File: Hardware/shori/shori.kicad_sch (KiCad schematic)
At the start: 50 parts, among them J1 Conn_02x03_Top_Bottom, J2 SWD_Header, J3 UART_Header, J5 AudioJack3, U1 STM32F405RGT6, U2 AP2112K-3.3, U3 PCM3060PWR, U4 NE5532, Y1 16MHz

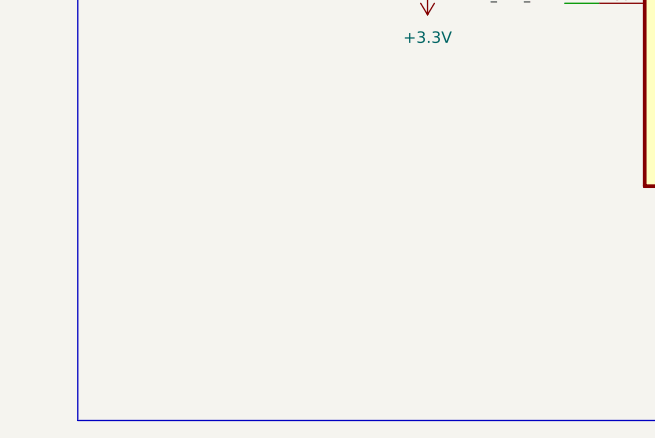
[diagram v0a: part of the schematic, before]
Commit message: Proper Border outline made for shori
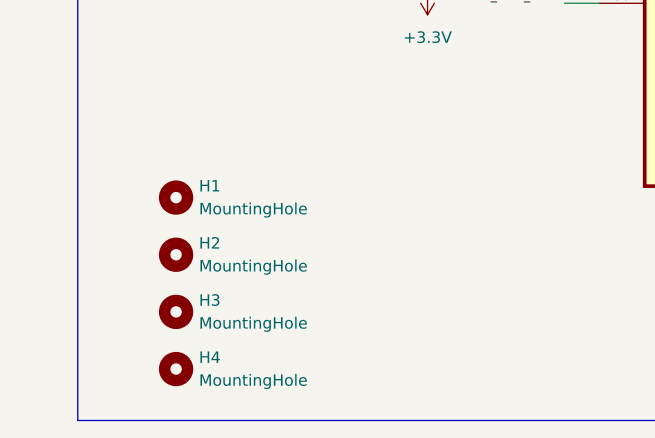
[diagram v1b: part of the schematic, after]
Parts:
- added H1, H2, H3, H4: MountingHole, MountingHole:MountingHole_3mm, symbol Mechanical:MountingHole

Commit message: saved previous commit
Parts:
- removed J1: Conn_02x03_Top_Bottom, Connector_IDC:IDC-Header_2x03_P2.54mm_Vertical, symbol Connector_Generic:Conn_02x03_Top_Bottom
- removed U1: STM32F405RGT6, My footprints:QFP50P1200X1200X160-64N, symbol STM32F4:STM32F405RGT6
- removed U2: AP2112K-3.3, Package_TO_SOT_SMD:SOT-23-5, symbol Regulator_Linear:AP2112K-3.3
- added C30: 10uF, Capacitor_SMD:C_0805_2012Metric, symbol Device:C
- added J1, J4, J6: Conn_01x03, Connector_JST:JST_EH_S3B-EH_1x03_P2.50mm_Horizontal, symbol Connector_Generic:Conn_01x03
- added U2: STM32H750VBTx, Package_QFP:LQFP-100_14x14mm_P0.5mm, symbol MCU_ST_STM32H7:STM32H750VBTx
- added U5: TPS73733DCQR, MyFootprints:IC_TPS73733DCQR, symbol TI LDO:TPS73733DCQR
- C10: value 10uF -> 100uF
- C3: value 10μF -> 4.7uF
- J3: footprint Connector_JST:JST_XH_B4B-XH-A_1x04_P2.50mm_Vertical -> Connector_JST:JST_XH_S4B-XH-A-1_1x04_P2.50mm_Horizontal
- U3: footprint My footprints:SOP65P640X120-28N -> MyFootprints:SOP65P640X120-28N
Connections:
- net NRST is gone; now on net BOOT0_R: C12.1, U3.15 (~{RST})
- net +3.3V: now also C30.1, U5.2 (OUT)
- net +3.3VA: now also U2.21 (VDDA)
- net BOOT0_R: now also U2.14 (NRST), U2.94 (BOOT0)
- net GND: now also C30.2, U2.10 (VSS), U2.100 (VDD), U2.11 (VDD), U2.19 (VSSA), U2.26 (VSS), U2.27 (VDD), U2.49 (VSS), U2.50 (VDD), U2.74 (VSS), U2.75 (VDD), U2.99 (VSS), U5.3 (GND_3), U5.6 (GND_6)
- net I2C_SCL: now also U2.46 (PB10)
- net I2C_SDA: now also U2.47 (PB11)
- net I2S_ADC_DATA: now also U2.53 (PB14)
- net I2S_BCLK: now also U2.51 (PB12)
- net I2S_DAC_DATA: now also U2.54 (PB15)
- net I2S_LRCLK: now also U2.52 (PB13)
- net I2S_MCLK: now also U2.63 (PC6)
- net SWCLK: now also U2.72 (PA13)
- net SWDIO: now also U2.76 (PA14)
- net UART_RX: now also J3.2 (Pin_2), U2.23 (PA1); no longer J3.3 (Pin_3)
- net UART_TX: now also J3.3 (Pin_3), U2.22 (PA0); no longer J3.2 (Pin_2)
- net VCAP_1: now also U2.48 (VCAP)
- net VCAP_2: now also U2.73 (VCAP)
- net at C3.1, D1.1 (K): now also U5.1 (IN), U5.5 (EN)
- no-connect marks 43 -> 6
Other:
- note added: "Shoyu Connectors: Power + AudioIn + AudioOut"
- note removed: "Main IDC Ribbon connector"
- moved on the sheet: C1, C10, C11, C12, C13, C14, C15, C16, C17, C18, C19, C2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

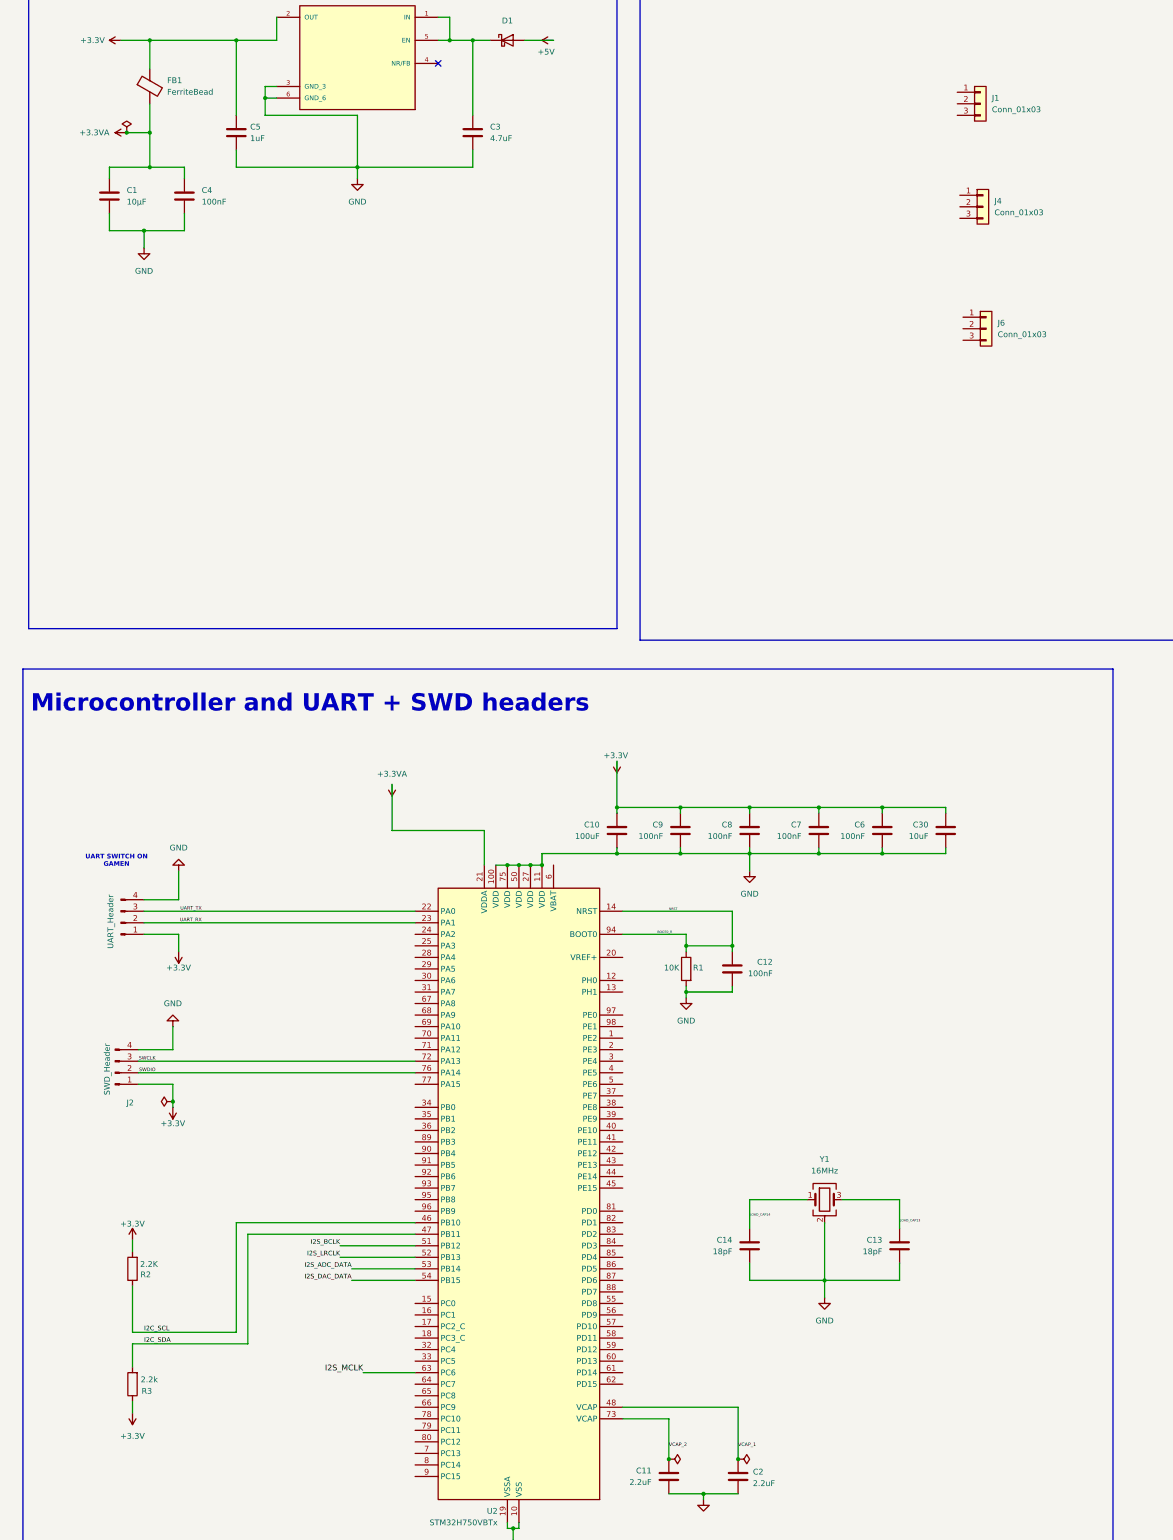
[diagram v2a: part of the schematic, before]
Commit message: Rev 2 mcu data lines and new shoyu molex connectors
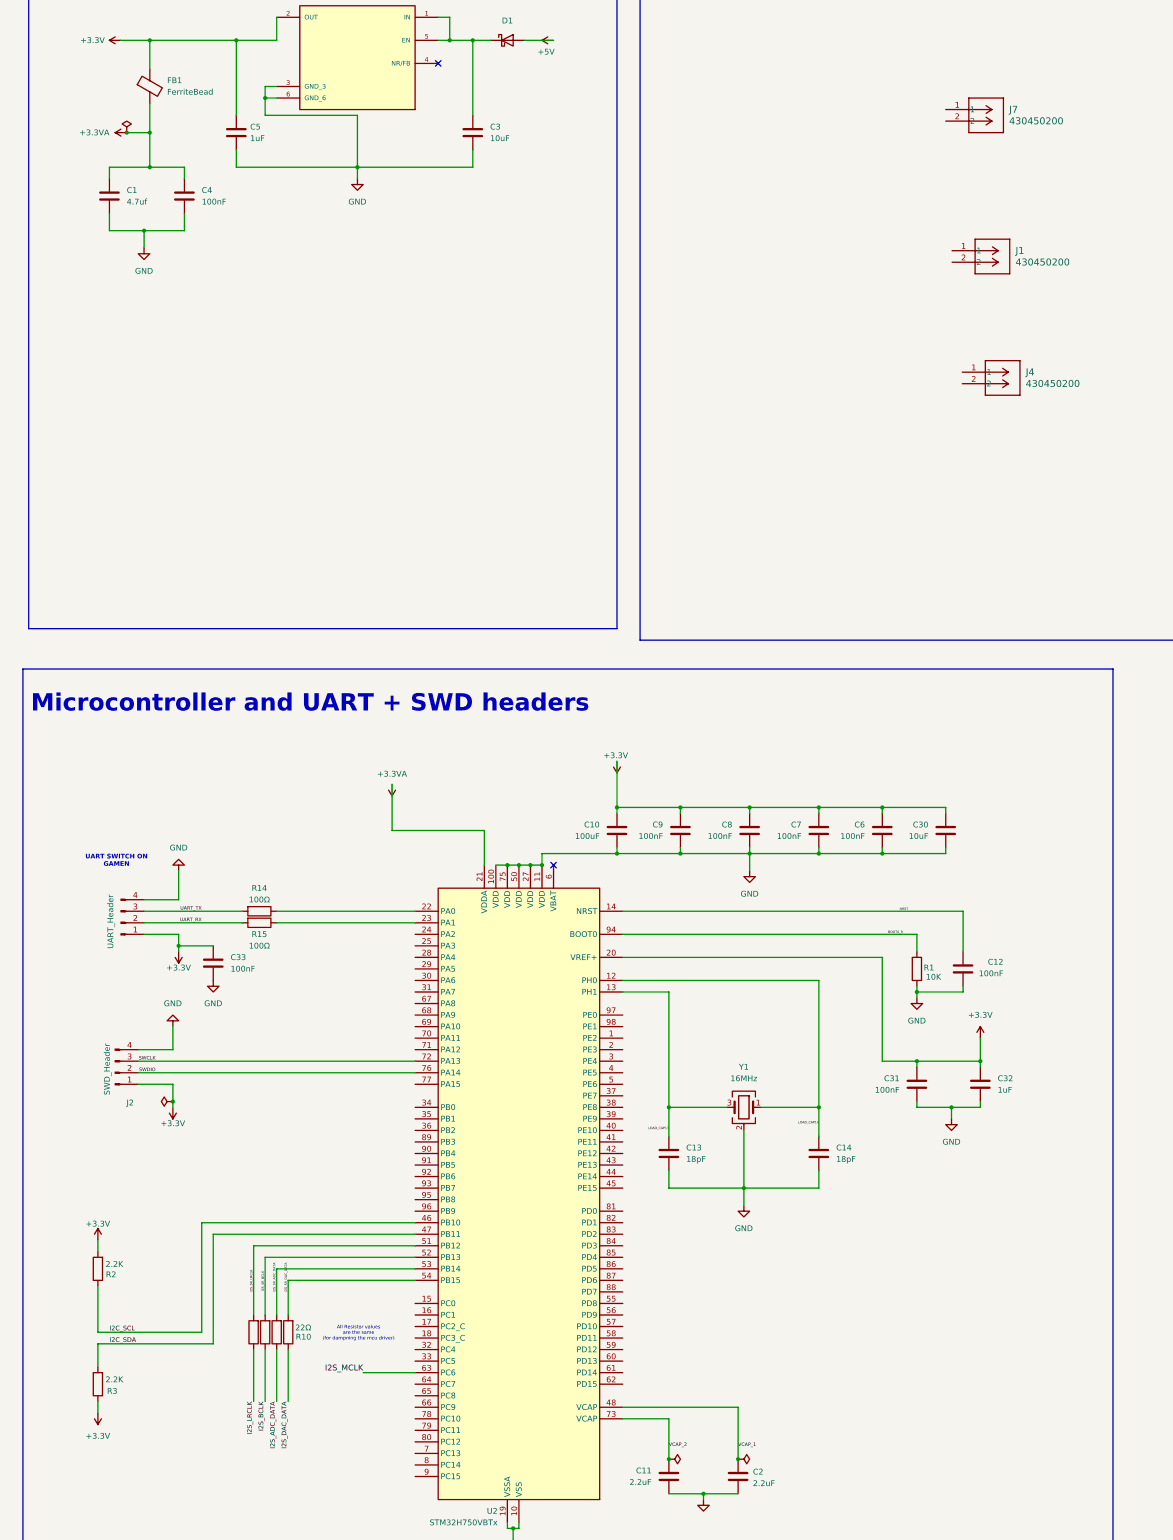
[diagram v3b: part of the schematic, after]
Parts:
- removed J1, J4, J6: Conn_01x03, Connector_JST:JST_EH_S3B-EH_1x03_P2.50mm_Horizontal, symbol Connector_Generic:Conn_01x03
- added C31: 100nF, Capacitor_SMD:C_0805_2012Metric, symbol Device:C
- added C32: 1uF, Capacitor_SMD:C_0805_2012Metric, symbol Device:C
- added C33: 100nF, symbol Device:C
- added J1, J4, J7: 430450200, MyFootprints:CONN_SD-43045-001_02_MOL, symbol MyConnectors:430450200
- added R10: 22Ω, Resistor_SMD:R_0805_2012Metric, symbol Device:R
- added R11, R12, R13: 22o, Resistor_SMD:R_0805_2012Metric, symbol Device:R
- added R14, R15: 100Ω, symbol Device:R
- C1: value 10μF -> 4.7uf
- C3: value 4.7uF -> 10uF
- R3: value 2.2k -> 2.2K
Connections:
- net +3.3V: now also U2.20 (VREF+), C31.1, C32.1, C33.1
- net BOOT0_R: no longer C12.1, U2.14 (NRST), U3.15 (~{RST})
- net GND: now also C31.2, C32.2, C33.2
- net I2S_ADC_DATA: now also R11.1; no longer U2.53 (PB14)
- net I2S_BCLK: now also R12.1; no longer U2.51 (PB12)
- net I2S_DAC_DATA: now also R10.1; no longer U2.54 (PB15)
- net I2S_LRCLK: now also R13.1; no longer U2.52 (PB13)
- net LOAD_CAP13: now also U2.13 (PH1)
- net LOAD_CAP14: now also U2.12 (PH0)
- net UART_RX: now also R15.2; no longer U2.23 (PA1)
- net UART_TX: now also R14.2; no longer U2.22 (PA0)
- new net: R15.1, U2.23 (PA1)
- new net: R14.1, U2.22 (PA0)
- new net I2S_SR_ADC_DATA: R11.2, U2.53 (PB14)
- new net I2S_SR_BCLK: R12.2, U2.52 (PB13)
- new net I2S_SR_DAC_DATA: R10.2, U2.54 (PB15)
- new net I2S_SR_LRCLK: R13.2, U2.51 (PB12)
- new net NRST: C12.1, U2.14 (NRST), U3.15 (~{RST})
- no-connect marks 6 -> 7
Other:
- note added: "All Resistor values are the same (for dampning the mcu driver)"
- moved on the sheet: C12, C13, C14, R1, R2, R3, Y1

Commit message: Shori Rev 2 schems complete!!!!!!
next is to add passive cvalues in the codec output filtering and assigning footprints
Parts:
- removed J4, J7: 430450200, MyFootprints:CONN_SD-43045-001_02_MOL, symbol MyConnectors:430450200
- removed U3: PCM3060PWR, MyFootprints:SOP65P640X120-28N, symbol TI Audio Codec:PCM3060PWR
- added C34: 0.1uF, Capacitor_SMD:C_0805_2012Metric, symbol Device:C
- added C35: 1μF, Capacitor_SMD:C_1206_3216Metric, symbol Device:C
- added C36: 2700pF, symbol Device:C
- added C37, C38: 470pF, symbol Device:C
- added C39: 0.01uF, symbol Device:C
- added C40, C41: 10uF, symbol Device:C
- added C42, C43, C44, C45, C46: C, symbol Device:C
- added J4: 530480310, My footprints:MOLEX_530480310, symbol Audio Molex:530480310
- added J6: 530480210, My footprints:CONN02_530480210_MOL, symbol 2 Pin Audio Molex:530480210
- added R16, R17, R32, R33: 1K, symbol Device:R
- added R18, R19: 91Ω, symbol Device:R
- added R20, R21: 634Ω, symbol Device:R
- added R22, R23: 10K, symbol Device:R
- added R24, R25, R26, R27, R28, R29, R30, R31: R, symbol Device:R
- added U1: CS4272, Package_SO:TSSOP-28_4.4x9.7mm_P0.65mm, symbol Audio:CS4272
- added U3: NE5532, Package_SO:SOIC-8_3.9x4.9mm_P1.27mm, symbol Amplifier_Operational:NE5532
- added U6: OPA134, Package_TO_SOT_SMD:SOT-23-5_HandSoldering, symbol Amplifier_Operational:OPA134
- C19: value 10μF -> 1μF
- C20: value 100nF -> 0.1uF
- C21: value 4.7μF -> 0.1uF
- C22: value 10μF -> C; footprint Capacitor_SMD:C_1206_3216Metric -> (none)
- C23: value 4.7μF -> 47uF; footprint Capacitor_SMD:C_0805_2012Metric -> Capacitor_SMD:C_1206_3216Metric
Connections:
- net AUDIO_IN is gone; now on net GND: C21.2
- net VINR is gone; now on net FILT+: C23.1
- net VOUTL+ is gone; now on net GND: C22.1
- net +3.3V: now also C34.1, C35.1, U1.10 (VL), U1.9 (VD)
- net +5V: now also J1.1
- net +5VA: now also U1.20 (VA), U3.8 (V+), U6.7 (V+)
- net AUDIO_OUT: now also J6.1; no longer C29.2
- net CODEC_DAC_OUT: now also R30.2, R31.2; no longer C22.2
- net GND: now also J1.2, C34.2, C35.2, C39.2, C42.1, C44.2, C46.2, J4.3, J6.2, R16.1, R17.1, R31.1, R32.1, R33.1, U1.13 (AD0/~{CS}(I2S/~{LJ})), U1.21 (AGND), U1.8 (DGND), U3.4 (V-), U6.4 (V-)
- net I2C_SCL: now also U1.11 (SCL/CCLK(M0))
- net I2C_SDA: now also U1.12 (SDA/CDIN(M1))
- net I2S_ADC_DATA: now also U1.6 (SDOUT(M/~{S}))
- net I2S_BCLK: now also U1.5 (SCLK)
- net I2S_DAC_DATA: now also U1.7 (SDIN)
- net I2S_LRCLK: now also U1.4 (LRCK)
- net I2S_MCLK: now also U1.3 (MCLK)
- net NRST: now also U1.14 (~{RST})
- net VCOM: now also C39.1, R22.1, R23.2, U1.15 (VCOM), U1.18 (AINB+), U1.19 (AINB-)
- net UART_RX_RES: now reaches R15.1, U2.23 (PA1)
- net UART_TX_RES: now reaches R14.1, U2.22 (PA0)
- net VINL renamed FILT+
- net FILT+: now also U1.22 (FILT+)
- new net: C43.1, C45.2, R28.2, U6.6
- new net: C43.2, R30.1
- new net: C37.1, R18.2, U3.1
- new net: C37.2, R20.2, U3.2 (-)
- new net: C40.1, R22.2, U3.3 (+)
- new net: R17.2, U1.26 (AOUTB+)
- new net: C22.2, R24.1, R25.2, R29.1
- new net: C38.2, R21.2, U3.6 (-)
- new net: C41.1, R23.1, U3.5 (+)
- new net: C38.1, R19.2, U3.7
- new net: C45.1, R27.2, U6.2 (-)
- new net: C46.1, R29.2
- new net: R16.2, U1.27 (AOUTB-)
- new net: C44.1, R24.2, U6.3 (+)
- new net: R33.2, U1.23 (~{AMUTEC})
- new net: R32.2, U1.28 (~{BMUTEC})
- new net: C42.2, R26.2, R27.1, R28.1
- new net AUDIO_IN+: C40.2, J4.1
- new net AUDIO_IN-: C41.2, J4.2
- new net CODEC_AIN+: C36.1, R18.1, R20.1, U1.17 (AINA+)
- new net CODEC_AIN-: C36.2, R19.1, R21.1, U1.16 (AINA-)
- new net CODEC_AOUT+: R25.1, U1.25 (AOUTA+)
- new net CODEC_AOUT-: R26.1, U1.24 (AOUTA-)
- no-connect marks 7 -> 75
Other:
- note added: "AUX Connectors And Mounting Holes"
- note added: "Input Filtering"
- note added: "Inverting Amplifier For Aux In"
- note added: "Output Filtering"
- note added: "Power Supply And Regulators"
- note added: "WAVEFORGE: SHORI REV 2"
- note removed: "AUX connector"
- note removed: "Inverting Amplifier For AUX In"
- note removed: "Power Input and Regulators"
- moved on the sheet: C10, C11, C12, C13, C14, C15, C16, C17, C18, C19, C2, C20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

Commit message: Added footprints for shori rev 2
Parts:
- C1, C30: footprint Capacitor_SMD:C_0805_2012Metric -> Capacitor_SMD:C_0603_1608Metric_Pad1.08x0.95mm_HandSolder
- C10, C19, C35: footprint Capacitor_SMD:C_1206_3216Metric -> Capacitor_SMD:C_0402_1005Metric_Pad0.74x0.62mm_HandSolder
- C11, C12, C13, C14, C16, C18, C2, C20, C21, C24, C25, C26, C27, C28, C31, C32, C34, C4, C5, C6, C7, C8, C9: footprint Capacitor_SMD:C_0805_2012Metric -> Capacitor_SMD:C_0402_1005Metric_Pad0.74x0.62mm_HandSolder
- C15, C17, C29, C3: footprint Capacitor_SMD:C_1206_3216Metric -> Capacitor_SMD:C_0603_1608Metric_Pad1.08x0.95mm_HandSolder
- C22: value C -> 6.8nF; footprint (none) -> Capacitor_SMD:C_0402_1005Metric_Pad0.74x0.62mm_HandSolder
- C23: footprint Capacitor_SMD:C_1206_3216Metric -> Capacitor_SMD:C_0805_2012Metric
- C33, C36, C37, C38, C39: footprint (none) -> Capacitor_SMD:C_0402_1005Metric_Pad0.74x0.62mm_HandSolder
- C40, C41: footprint (none) -> Capacitor_SMD:C_0603_1608Metric_Pad1.08x0.95mm_HandSolder
- C42: value C -> 2200pF; footprint (none) -> Capacitor_SMD:C_0402_1005Metric_Pad0.74x0.62mm_HandSolder
- C43, C46: value C -> 22uF; footprint (none) -> Capacitor_SMD:C_0805_2012Metric
- C44: value C -> 1.5nF; footprint (none) -> Capacitor_SMD:C_0402_1005Metric_Pad0.74x0.62mm_HandSolder
- C45: value C -> 470pF; footprint (none) -> Capacitor_SMD:C_0402_1005Metric_Pad0.74x0.62mm_HandSolder
- R1, R10, R2, R3, R4, R5, R6, R7, R8, R9: footprint Resistor_SMD:R_0805_2012Metric -> Resistor_SMD:R_0402_1005Metric_Pad0.72x0.64mm_HandSolder
- R11, R12, R13: value 22o -> 22Ω; footprint Resistor_SMD:R_0805_2012Metric -> Resistor_SMD:R_0402_1005Metric_Pad0.72x0.64mm_HandSolder
- R14, R15, R16, R17, R18, R19, R20, R21, R22, R23, R32, R33: footprint (none) -> Resistor_SMD:R_0402_1005Metric_Pad0.72x0.64mm_HandSolder
- R24: value R -> 715Ω; footprint (none) -> Resistor_SMD:R_0402_1005Metric_Pad0.72x0.64mm_HandSolder
- R25: value R -> 1.33K; footprint (none) -> Resistor_SMD:R_0402_1005Metric_Pad0.72x0.64mm_HandSolder
- R26: value R -> 4.42K; footprint (none) -> Resistor_SMD:R_0402_1005Metric_Pad0.72x0.64mm_HandSolder
- R27: value R -> 2.32K; footprint (none) -> Resistor_SMD:R_0402_1005Metric_Pad0.72x0.64mm_HandSolder
- R28: value R -> 4.99K; footprint (none) -> Resistor_SMD:R_0402_1005Metric_Pad0.72x0.64mm_HandSolder
- R29: value R -> 1.5K; footprint (none) -> Resistor_SMD:R_0402_1005Metric_Pad0.72x0.64mm_HandSolder
- R30: value R -> 560Ω; footprint (none) -> Resistor_SMD:R_0402_1005Metric_Pad0.72x0.64mm_HandSolder
- R31: value R -> 47K; footprint (none) -> Resistor_SMD:R_0402_1005Metric_Pad0.72x0.64mm_HandSolder
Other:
- note added: "Audio Goes back to shoyu as a single signal from the aux circuit"
- note added: "Audio goes into the codec input buffer as a differential pair"
- note added: "COG PERCISION CAPS: C36 C38 C37"
- note added: "COG PERCISION CAPS: C45 C42 C22 C44"
- note added: "Inverting Amplifier Aux Circuit"
- note added: "Main +5V rail comes in from shoyu"
- note removed: "Inverting Amplifier For Aux In"
- moved on the sheet: J1, J4, J6

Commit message: New I2S2 Pinout and MCLK resistor added
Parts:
- added R34: 22Ω, Resistor_SMD:R_0402_1005Metric_Pad0.72x0.64mm_HandSolder, symbol Device:R
- R10: value 22Ω -> 100Ω
- R15: value 100Ω -> 22Ω
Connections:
- net AUDIO_OUT: now also C29.2
- net I2S_LRCLK: now also R15.2; no longer R13.1
- net I2S_MCLK: now also R34.2; no longer U2.63 (PC6)
- net UART_RX: now also R10.2; no longer R15.2
- net UART_RX_RES: now also R10.1; no longer R15.1
- net I2S_SCLK_RES: now reaches U2.68 (PA9)
- net I2S_SCLK_RES: now also R11.1
- net I2S_LRCLK_RES: now reaches U2.70 (PA11)
- net I2S_LRCLK_RES: now also R15.1
- net I2S_ADC_DATA renamed CODEC_SDOUT
- net CODEC_SDOUT: now also R12.2; no longer R11.1
- net I2S_BCLK renamed I2S_CODEC_SDOUT_RES
- net I2S_CODEC_SDOUT_RES: now also U2.53 (PB14); no longer U1.5 (SCLK)
- net I2S_DAC_DATA renamed CODEC_SDIN
- net CODEC_SDIN: now also R13.2; no longer R10.1
- net I2S_SR_ADC_DATA renamed I2S_SCLK
- net I2S_SCLK: now also U1.5 (SCLK); no longer U2.53 (PB14)
- net I2S_SR_BCLK: no longer names the net of U2.52 (PB13)
- net I2S_SR_BCLK: no longer R12.2
- net I2S_SR_DAC_DATA renamed I2S_CODEC_SDIN_RES
- net I2S_CODEC_SDIN_RES: now also R13.1; no longer R10.2
- net I2S_SR_LRCLK: no longer names the net of U2.51 (PB12)
- net I2S_SR_LRCLK: no longer R13.2
- new net I2S_MCLK_RES: R34.1, U2.63 (PC6)
- no-connect marks 75 -> 76
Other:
- note removed: "All Resistor values are the same (for dampning the mcu driver)"
- moved on the sheet: R15

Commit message: Fixed Stupid mistakes and began power and mcu layout
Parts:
- C10: value 100uF -> 100nF
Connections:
- net +3.3V: now also U2.100 (VDD), U2.11 (VDD), U2.27 (VDD), U2.50 (VDD), U2.75 (VDD)
- net GND: no longer U2.100 (VDD), U2.11 (VDD), U2.27 (VDD), U2.50 (VDD), U2.75 (VDD)
- net LOAD_CAP13: now also Y1.1; no longer Y1.3
- net LOAD_CAP14: now also Y1.3; no longer Y1.1
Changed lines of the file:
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@@
 	)
 	(junction
-		(at 156.21 231.14)
-		(diameter 0)
-		(color 0 0 0 0)
-	)
-	(junction
 		(at 415.29 248.92)
 		(diameter 0)
@@
 	(wire
 		(pts
-			(xy 139.7 231.14) (xy 156.21 231.14)
-		)
-		(stroke
-			(width 0)
-			(type default)
-		)
-	)
-	(wire
-		(pts
 			(xy 560.07 332.74) (xy 552.45 332.74)
 		)
@@
 	(wire
 		(pts
-			(xy 139.7 233.68) (xy 139.7 231.14)
+			(xy 139.7 220.98) (xy 139.7 233.68)
 		)
 		(stroke
@@
 	(wire
 		(pts
+			(xy 139.7 220.98) (xy 156.21 220.98)
+		)
+		(stroke
+			(width 0)
+			(type default)
+		)
+	)
+	(wire
+		(pts
 			(xy 560.07 346.71) (xy 560.07 342.9)
 		)
@@
 		(on_board yes)
 		(dnp no)
-		(fields_autoplaced yes)
 		(property "Reference" "C10"
-			(at 152.4 224.7899 0)
+			(at 147.574 224.536 0)
 			(effects
 				(font
 					(size 1.27 1.27)
 				)
-				(justify left)
+				(justify right)
 			)
 		)
-		(property "Value" "100uF"
-			(at 152.4 227.3299 0)
+		(property "Value" "100nF"
+			(at 147.574 227.076 0)
 			(effects
 				(font
 					(size 1.27 1.27)
 				)
-				(justify left)
+				(justify right)
 			)
 		)
@@
 		(lib_id "Device:Crystal_GND24")
 		(at 184.15 287.02 0)
-		(mirror y)
 		(unit 1)
 		(exclude_from_sim no)
